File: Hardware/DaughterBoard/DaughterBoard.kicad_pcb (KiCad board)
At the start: 2 copper layers, 145 x 160 mm, 54 parts, among them J1 CARTDRIGE, J10 JOYPAD2, J11 LCD, J12 POWER, J13 PA, J14 PB, J2 ROM, J3 ISA00, J4 ISA10, J5 AUDIO_OUT, J6 VGA_OUT, J7 ISA01, J8 ISA11, J9 JOYPAD1, U1 ATmega328P-PU, U2 ATmega1284P-PU, U4 ATmega328P-PU, U5 HM62256BLP, U6 74LS365, X1 ACO-20MHz

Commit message: Version 1.2
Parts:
- removed the H4 at (84.3, 144.3)
- removed the H4 at (163.3, 144.3)
- removed R10, R11, R3, R4, R5, R6, R7, R8, R9: 10K, Resistor_THT:R_Axial_DIN0207_L6.3mm_D2.5mm_P10.16mm_Horizontal
- removed Xiaoniuniu: LOGO, Logos:SmallCow
- added XiaoNiuNiu: LOGO, Logos:SmallCow, F.Cu at (140.7, 88.4)
- J1: footprint Connector_PinSocket_2.54mm:PinSocket_2x30_P2.54mm_Vertical -> Connector_PinHeader_2.54mm:PinHeader_2x15_P2.54mm_Vertical
- J10, J9: footprint Connector_PinSocket_2.54mm:PinSocket_2x04_P2.54mm_Vertical -> Connector_TheRLab:NES_JoyPad
- J11: footprint Connector_PinHeader_2.54mm:PinHeader_2x07_P2.54mm_Vertical -> Connector_IDC:IDC-Header_2x10_P2.54mm_Vertical
- U5: value HM62256BLP -> AS6C62256
- U6: value 74LS365 -> 74HC365
- moved J9 14.7 mm to (45.0, 84.6)
- moved J10 13.6 mm to (45.0, 55.6)
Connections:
- J1 pad 1: /A14 -> Net-(J1-Pad1)
- J1 pad 11: /A4 -> Net-(J1-Pad11)
- J1 pad 13: /A3 -> Net-(J1-Pad13)
- J1 pad 14: Net-(J1-Pad14) -> GND
- J1 pad 15: /A2 -> Net-(J1-Pad15)
- J1 pad 17: /A1 -> Net-(J1-Pad17)
- J1 pad 19: /A0 -> Net-(J1-Pad19)
- J1 pad 21: no_connect_121 -> Net-(J1-Pad21)
- J1 pad 22: no_connect_122 -> Net-(J1-Pad22)
- J1 pad 23: /D0 -> Net-(J1-Pad23)
- J1 pad 25: /D1 -> Net-(J1-Pad25)
- J1 pad 27: /D2 -> +5V
- J1 pad 28: Net-(J1-Pad28) -> +5V
- J1 pad 3: /A12 -> Net-(J1-Pad3)
- J1 pad 5: /A7 -> Net-(J1-Pad5)
- J1 pad 7: /A6 -> Net-(J1-Pad7)
- J1 pad 9: /A5 -> Net-(J1-Pad9)
- J10 pad 1: JP_DATA2 -> GND
- J10 pad 2: no_connect_123 -> JP_CLOCK
- J10 pad 3: GND -> JP_LATCH2
- J10 pad 4: +5V -> JP_DATA2
- J10 pad 5: JP_CLOCK -> (no net)
- J10 pad 6: JP_LATCH2 -> (no net)
- J10 pad 7: (no net) -> +5V
- J11 pad 10: LCD_D7 -> LCD_D5
- J11 pad 12: no_connect_124 -> LCD_D6
- J11 pad 14: GND -> LCD_D7
- J11 pad 2: LCD_D3 -> CB1
- J11 pad 4: LCD_D4 -> CB2
- J11 pad 6: LCD_D5 -> LCD_D3
- J11 pad 8: LCD_D6 -> LCD_D4
- J13 pad 10: Net-(J13-Pad10) -> CA2
- J13 pad 9: Net-(J13-Pad9) -> CA1
- J14 pad 10: Net-(J14-Pad10) -> CB2
- J14 pad 9: Net-(J14-Pad9) -> CB1
- J2 pad 1: Net-(J1-Pad2) -> Net-(J1-Pad1)
- J2 pad 10: Net-(J1-Pad20) -> Net-(J1-Pad10)
- J2 pad 11: Net-(J1-Pad24) -> Net-(J1-Pad11)
- J2 pad 12: Net-(J1-Pad26) -> Net-(J1-Pad12)
- J2 pad 13: Net-(J1-Pad28) -> Net-(J1-Pad13)
- J2 pad 15: Net-(J1-Pad32) -> Net-(J1-Pad15)
- J2 pad 16: Net-(J1-Pad34) -> Net-(J1-Pad16)
- J2 pad 17: Net-(J1-Pad36) -> Net-(J1-Pad17)
- J2 pad 18: Net-(J1-Pad38) -> Net-(J1-Pad18)
- J2 pad 19: Net-(J1-Pad40) -> Net-(J1-Pad19)
- J2 pad 2: Net-(J1-Pad4) -> Net-(J1-Pad2)
- J2 pad 20: Net-(J1-Pad42) -> Net-(J1-Pad20)
- J2 pad 21: Net-(J1-Pad44) -> Net-(J1-Pad21)
- J2 pad 22: Net-(J1-Pad46) -> Net-(J1-Pad22)
- J2 pad 23: Net-(J1-Pad48) -> Net-(J1-Pad23)
- J2 pad 24: Net-(J1-Pad50) -> Net-(J1-Pad24)
- J2 pad 25: Net-(J1-Pad52) -> Net-(J1-Pad25)
- J2 pad 26: Net-(J1-Pad54) -> Net-(J1-Pad26)
- J2 pad 3: Net-(J1-Pad6) -> Net-(J1-Pad3)
- J2 pad 4: Net-(J1-Pad8) -> Net-(J1-Pad4)
- J2 pad 5: Net-(J1-Pad10) -> Net-(J1-Pad5)
- J2 pad 6: Net-(J1-Pad12) -> Net-(J1-Pad6)
- J2 pad 7: Net-(J1-Pad14) -> Net-(J1-Pad7)
- J2 pad 8: Net-(J1-Pad16) -> Net-(J1-Pad8)
- J2 pad 9: Net-(J1-Pad18) -> Net-(J1-Pad9)
- J3 pad 11: no_connect_125 -> /IRQ0B
- J3 pad 15: +5V -> GND
- J3 pad 16: no_connect_126 -> +5V
- J4 pad 15: +5V -> /RDYB
- J4 pad 16: /RDYB -> +5V
- J6 pad 11: no_connect_127 -> (no net)
- J6 pad 12: no_connect_128 -> (no net)
- J6 pad 15: no_connect_129 -> (no net)
- J6 pad 4: no_connect_130 -> (no net)
- J6 pad 9: no_connect_131 -> (no net)
- J7 pad 10: /A09 -> (no net)
- J7 pad 11: /A010 -> (no net)
- J7 pad 12: /A011 -> (no net)
- J7 pad 13: /A012 -> (no net)
- J7 pad 14: /A013 -> (no net)
- J7 pad 15: /A014 -> (no net)
- J7 pad 16: GND -> (no net)
- J7 pad 7: /A06 -> (no net)
- J7 pad 8: /A07 -> (no net)
- J7 pad 9: /A08 -> (no net)
- J9 pad 1: JP_DATA1 -> GND
- J9 pad 2: no_connect_132 -> JP_CLOCK
- J9 pad 3: GND -> JP_LATCH1
- J9 pad 4: +5V -> JP_DATA1
- J9 pad 5: JP_CLOCK -> (no net)
- J9 pad 6: JP_LATCH1 -> (no net)
- J9 pad 7: (no net) -> +5V
- U1 pad 10: no_connect_133 -> (no net)
- U1 pad 14: no_connect_134 -> (no net)
- U1 pad 19: no_connect_135 -> /IRQ0B
- U2 pad 1: ROMB -> /RDYB
- U2 pad 12: no_connect_136 -> (no net)
- U2 pad 33: no_connect_137 -> (no net)
- U2 pad 8: no_connect_138 -> (no net)
- U4 pad 10: no_connect_139 -> (no net)
- U4 pad 19: /RDYB -> (no net)
- X1 pad 1: no_connect_140 -> (no net)
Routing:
- net ROMB: track 118.3 -> 0.00 mm, vias 2 -> 0
- net /A12: track 286.0 -> 171.8 mm, vias 6 -> 4
- net /A6: track 377.2 -> 278.1 mm, vias 6 -> 5
- net /A5: track 376.7 -> 279.7 mm, vias 6 -> 5
- net /A4: track 364.6 -> 270.1 mm, vias 6 -> 5
- net /IRQ0B: track 0.00 -> 92.7 mm
- net /A3: track 363.5 -> 271.2 mm, vias 6 -> 5
- net /A2: track 363.8 -> 272.3 mm, vias 6 -> 5
- net /A1: track 364.1 -> 273.4 mm, vias 6 -> 5
- net /A7: track 362.0 -> 275.5 mm, vias 6 -> 5
- net /A0: track 348.5 -> 273.1 mm, vias 7 -> 5
- net CA2: track 0.00 -> 73.0 mm
- net CA1: track 0.00 -> 72.5 mm
- net /D0: track 381.9 -> 315.1 mm, vias 6 -> 4
- net /D1: track 375.8 -> 313.6 mm, vias 6 -> 4
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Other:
- board text added: "A15"
- board text added: "IRQ0B"
- board text added: "Miniish 1.2"
- board text added: "PA5"
- board text added: "PB2"
- board text added: "PB3"
- board text added: "RDYB"
- board text removed: "A14"
- board text removed: "Miniish 1.1"

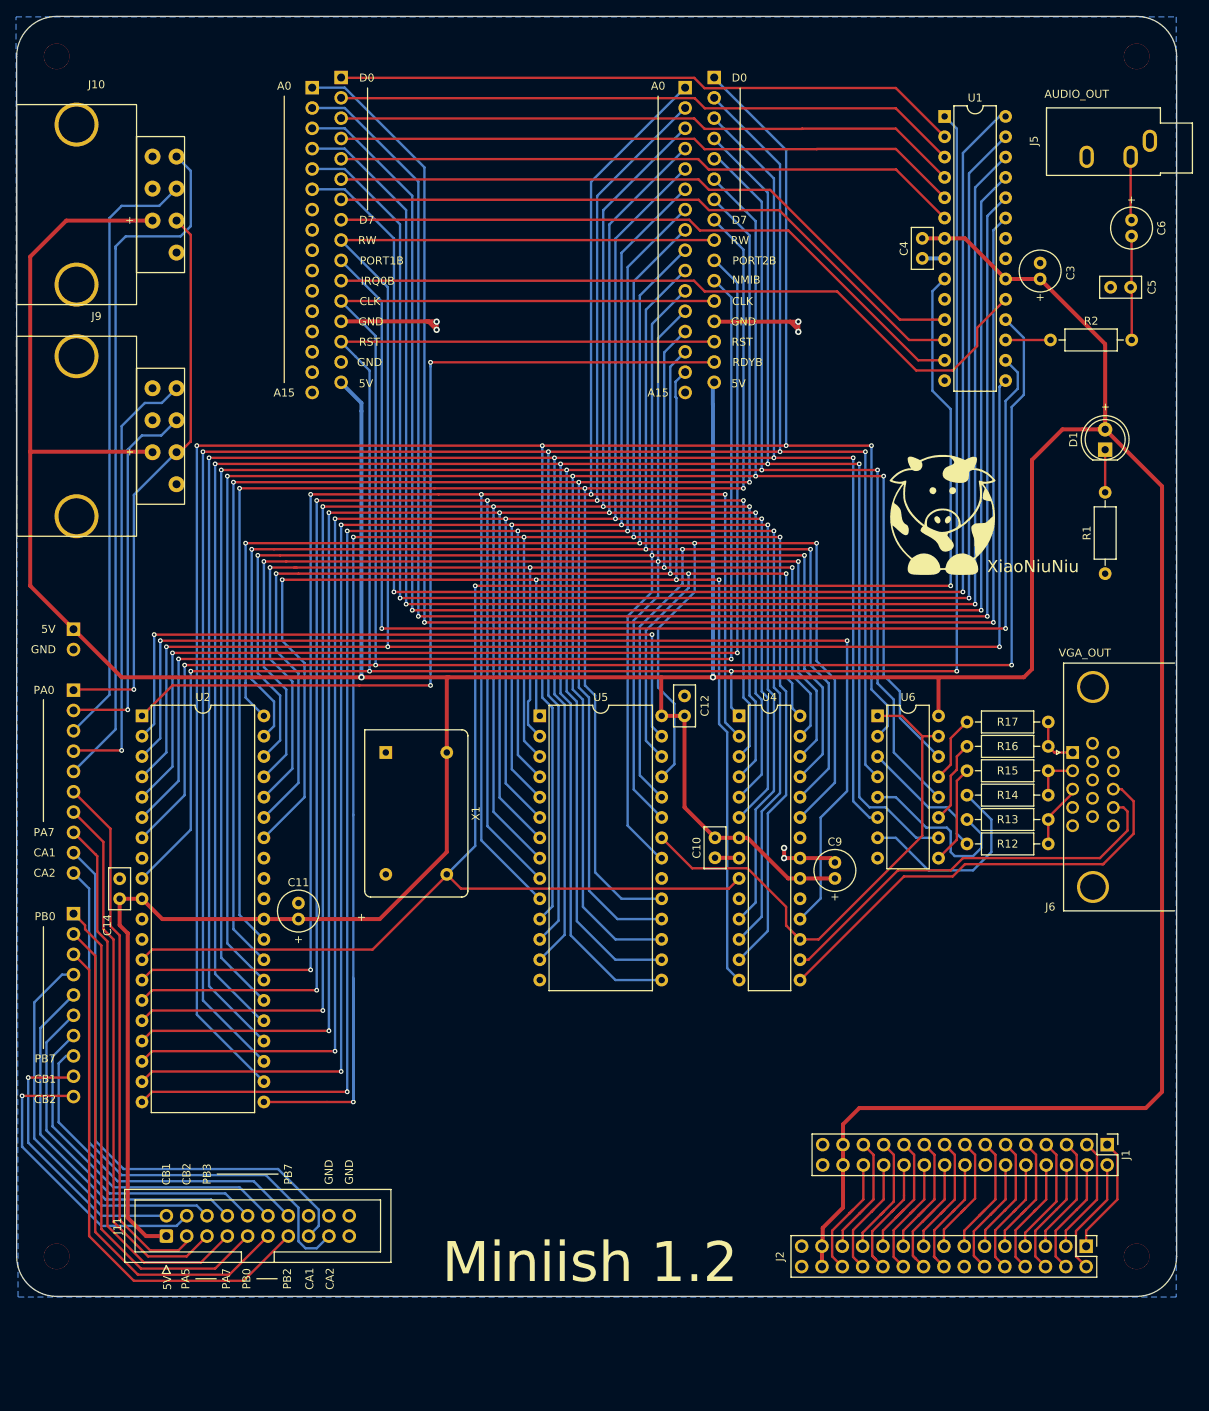
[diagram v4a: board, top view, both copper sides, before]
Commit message: New PLD logic, VGA, DMA ...
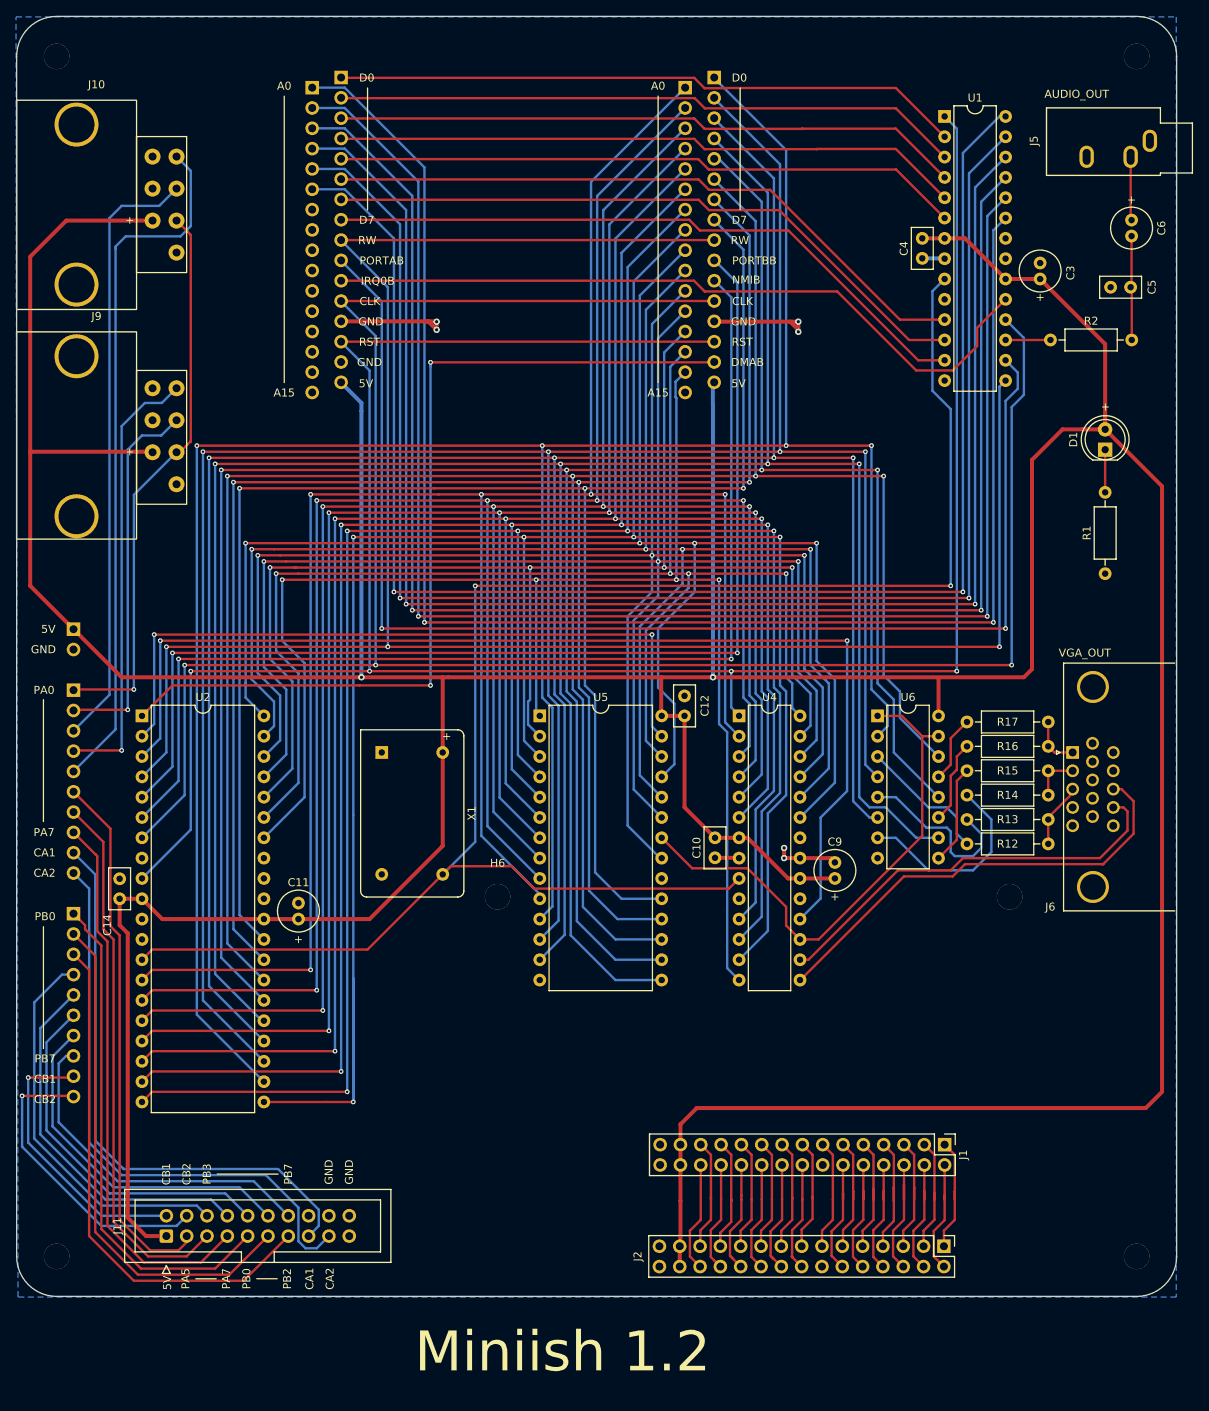
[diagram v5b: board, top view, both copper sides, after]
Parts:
- removed XiaoNiuNiu: LOGO, Logos:SmallCow
- added H5: MountingHole_Pad, MountingHole:MountingHole_3.2mm_M3, F.Cu at (149.1, 136.1)
- added H6: MountingHole_Pad, MountingHole:MountingHole_3.2mm_M3, F.Cu at (85.1, 136.1)
- moved J1 20.3 mm to (141.0, 167.1)
- moved J2 17.8 mm to (140.9, 179.8)
- moved X1 0.51 mm to (70.6, 118.1)
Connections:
- net /A0 renamed /AB0
- net /A00 renamed /AA0
- net /A01 renamed /AA1
- net /A02 renamed /AA2
- net /A03 renamed /AA3
- net /A04 renamed /AA4
- net /A05 renamed /AA5
- net /A1 renamed /AB1
- net /A10 renamed /AB10
- net /A11 renamed /AB11
- net /A12 renamed /AB12
- net /A13 renamed /AB13
- net /A14 renamed /AB14
- net /A2 renamed /AB2
- net /A3 renamed /AB3
- net /A4 renamed /AB4
- net /A5 renamed /AB5
- net /A6 renamed /AB6
- net /A7 renamed /AB7
- net /A8 renamed /AB8
- net /A9 renamed /AB9
- net /D0 renamed /DB0
- net /D00 renamed /DA0
- net /D01 renamed /DA1
- net /D02 renamed /DA2
- net /D03 renamed /DA3
- net /D04 renamed /DA4
- net /D05 renamed /DA5
- net /D06 renamed /DA6
- net /D07 renamed /DA7
- net /D1 renamed /DB1
- net /D2 renamed /DB2
- net /D3 renamed /DB3
- net /D4 renamed /DB4
- net /D5 renamed /DB5
- net /D6 renamed /DB6
- net /D7 renamed /DB7
- net /PORT1B renamed /PORTAB
- net /PORT2B renamed /PORTBB
- net /RDYB renamed /DMAB
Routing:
- net +5V: track 661.7 -> 680.0 mm
- net Net-(J1-Pad18): track 17.5 -> 14.3 mm
- net Net-(J1-Pad21): track 16.3 -> 13.8 mm
- net Net-(J1-Pad19): track 15.9 -> 13.8 mm
- net Net-(J1-Pad13): track 16.0 -> 13.8 mm
- net Net-(J1-Pad20): track 15.5 -> 13.7 mm
- net Net-(J1-Pad26): track 15.6 -> 13.8 mm
- net Net-(J1-Pad15): track 15.5 -> 13.9 mm
- net Net-(J1-Pad17): track 15.6 -> 14.0 mm
- net Net-(J1-Pad25): track 15.6 -> 14.0 mm
- net Net-(J1-Pad24): track 15.1 -> 13.7 mm
- net Net-(J1-Pad16): track 15.4 -> 14.0 mm
- net Net-(J1-Pad22): track 15.7 -> 14.3 mm
- net Net-(J1-Pad23): track 15.4 -> 14.0 mm
- net Net-(J1-Pad12): track 15.8 -> 14.6 mm
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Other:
- board text added: "DMAB"
- board text added: "PORTAB"
- board text added: "PORTBB"
- board text removed: "PORT1B"
- board text removed: "PORT2B"
- board text removed: "RDYB"
